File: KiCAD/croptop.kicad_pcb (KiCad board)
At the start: 4 copper layers, 152.4 x 53.3 mm, 286 parts, among them J1 PICKit Header, J2 USB_A, J3 5V USB, J4 4-1734839-0, J5 Terminal Block, J6 DNP, J7 DNP, SW1 BTNA, SW2 BTNA, SW3 BTNA, SW4 BTNA, U1 PIC32MX795F512L, U10 AD7799, U11 74HCT125D, U12 Si7006-A20, U13 UCAM-M8Q, U14 W25N01GV, U15 LIS3DH, U16 PUSBM5V5X4, U17 DT6250-06MR-13, U18 PUSBM5V5X4, U2 REG71055, U3 FAN5333BSX, U4 MIC23050, U5 TC1014, U6 FT812Q, U8 74HCT125D, U9 DRV8872, Y1 CXO, Y2 12MHz

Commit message: Dec 18th
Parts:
- removed C55: 100uF, Capacitor_SMD:CP_Elec_6.3x7.7
- removed C72: 0.1uF, Capacitor_SMD:C_0402_1005Metric
- removed R58, R59, R60, R61: 10k, Resistor_SMD:R_0402_1005Metric
- removed SW3, SW4: BTNA, Button_Switch_SMD:SW_SPST_PTS645
- removed TP93, TP94: TestPoint_Alt, TestPoint:TestPoint_Pad_D2.0mm
- D9: footprint Package_TO_SOT_SMD:TO-252-3_TabPin2 -> croptop:SizeOfThisLad
- moved R62 161.8 mm to (200.7, 84.5)
- moved R64 155.3 mm to (201.6, 66.5)
- moved R65 152.4 mm to (202.3, 69.0)
- moved R56 151.5 mm to (198.3, 84.0)
- moved R37 102.6 mm to (125.3, 122.0), turned to 270 degrees
- moved R67 94.2 mm to (200.5, 70.3)
- moved R66 88.8 mm to (199.3, 68.4)
- moved D9 86.3 mm to (117.1, 130.2), turned to 180 degrees
- moved R48 86.1 mm to (105.7, 125.5), turned to 180 degrees
- moved R63 85.3 mm to (200.7, 86.2)
- moved R36 83.9 mm to (125.3, 124.3), turned to 270 degrees
- moved R57 79.6 mm to (198.3, 86.4)
- moved U9 74.7 mm to (117.2, 123.1), turned to 180 degrees
- moved C42 74.5 mm to (206.7, 115.1)
- moved C47 73.7 mm to (122.9, 125.3), turned to 180 degrees
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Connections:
- U10 pad 5: Net-(C52-Pad1) -> Net-(C53-Pad1)
- U10 pad 6: Net-(C52-Pad2) -> Net-(C53-Pad2)
- U10 pad 7: Net-(C53-Pad1) -> Net-(C52-Pad1)
- U10 pad 8: Net-(C53-Pad2) -> Net-(C52-Pad2)
- U11 pad 2: Net-(R48-Pad1) -> ROT_A1
- U11 pad 3: ROT_A1 -> Net-(R48-Pad1)
- U11 pad 5: Net-(R49-Pad1) -> ROT_A2
- U11 pad 6: ROT_A2 -> Net-(R49-Pad1)
- U17 pad 3: Net-(J6-Pad4) -> ADC_A1-
- U17 pad 4: Net-(J6-Pad3) -> ADC_A1+
- U17 pad 5: ADC_A1- -> Net-(J6-Pad4)
- U17 pad 6: ADC_A1+ -> Net-(J6-Pad3)
- U5 pad 2: (no net) -> DRV_GND
- U6 pad 57: (no net) -> DRV_GND
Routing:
- net Net-(J7-Pad4): track 0.00 -> 25.4 mm, vias 0 -> 2
- net Net-(J7-Pad3): track 0.00 -> 24.4 mm, vias 0 -> 2
- net ROT_A2: track 0.00 -> 22.5 mm, vias 0 -> 6
- net ROT_VDD: track 0.00 -> 18.3 mm, vias 0 -> 2
- net ROT_A1: track 0.00 -> 16.9 mm, vias 0 -> 2
- net Net-(C54-Pad2): track 0.00 -> 15.8 mm, vias 0 -> 2
- net Net-(C54-Pad1): track 0.00 -> 15.6 mm, vias 0 -> 2
- net Net-(J6-Pad3): track 0.00 -> 11.7 mm, vias 0 -> 2
- net ADC_A1-: track 0.00 -> 11.3 mm, vias 0 -> 2
- net ADC_A1+: track 0.00 -> 10.2 mm, vias 0 -> 2
- net Net-(R39-Pad2): track 0.00 -> 10.1 mm, vias 0 -> 2
- net Net-(C52-Pad2): track 0.00 -> 9.97 mm, vias 0 -> 2
- net Net-(J4-Pad34): track 0.00 -> 9.70 mm
- net Net-(J4-Pad5): track 0.00 -> 9.65 mm
- net Net-(J4-Pad6): track 0.00 -> 9.36 mm
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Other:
- board size 152.4 x 53.3 mm -> 130.2 x 45.1 mm

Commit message: Dec 19th
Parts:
- moved C66 122.8 mm to (211.8, 118.1)
- moved C68 115.5 mm to (202.6, 127.0)
- moved U13 85.1 mm to (170.2, 103.5), turned to 180 degrees
- moved C42 77.5 mm to (135.0, 144.3)
- moved C41 77.5 mm to (132.2, 145.7)
- moved D22 73.7 mm to (146.6, 106.6)
- moved D24 73.7 mm to (142.2, 102.5)
- moved D25 73.7 mm to (142.5, 106.3)
- moved R64 73.7 mm to (138.1, 103.9)
- moved R65 73.7 mm to (138.8, 106.5)
- moved R66 73.7 mm to (135.8, 105.8)
- moved D23 73.7 mm to (146.0, 103.4)
- moved R67 73.7 mm to (137.0, 107.7)
- moved C3 61.9 mm to (108.1, 94.1)
- moved R27 61.9 mm to (115.1, 89.8)
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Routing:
- net LCD_G7: track 0.00 -> 30.3 mm, vias 0 -> 2
- net LCD_B6: track 0.00 -> 29.6 mm, vias 0 -> 2
- net LCD_DISP: track 0.00 -> 29.2 mm, vias 0 -> 2
- net LCD_DEN: track 0.00 -> 29.1 mm, vias 0 -> 2
- net LCD_SHIFT: track 0.00 -> 29.0 mm, vias 0 -> 2
- net LCD_B0: track 0.00 -> 29.0 mm, vias 0 -> 2
- net LCD_HSYNC: track 0.00 -> 29.0 mm, vias 0 -> 2
- net LCD_VSYNC: track 0.00 -> 28.8 mm, vias 0 -> 2
- net LCD_B7: track 0.00 -> 28.8 mm, vias 0 -> 2
- net LCD_B1: track 0.00 -> 28.8 mm, vias 0 -> 2
- net LCD_G6: track 0.00 -> 28.7 mm, vias 0 -> 2
- net LCD_B2: track 0.00 -> 28.5 mm, vias 0 -> 2
- net LCD_B3: track 0.00 -> 28.3 mm, vias 0 -> 2
- net LCD_B4: track 0.00 -> 28.1 mm, vias 0 -> 2
- net LCD_B5: track 0.00 -> 27.9 mm, vias 0 -> 2
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
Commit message: Before remove LCD resistors
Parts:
- moved R52 89.7 mm to (184.0, 94.7)
- moved R53 86.3 mm to (178.3, 91.6)
- moved C66 32.0 mm to (184.3, 101.9)
- moved C68 27.5 mm to (183.9, 106.8)
- moved C63 17.0 mm to (105.7, 124.0)
- moved C62 14.0 mm to (109.0, 123.7)
- moved C17 9.60 mm to (120.7, 85.9)
- moved C47 8.32 mm to (114.6, 125.2)
- moved U9 8.25 mm to (125.3, 121.7)
- moved R36 6.77 mm to (128.4, 118.3), turned to 180 degrees
- moved C42 6.51 mm to (131.6, 138.7), turned to 90 degrees
- moved R37 5.72 mm to (128.4, 117.2), turned to 180 degrees
- moved U6 4.42 mm to (141.9, 121.4)
- moved C33 4.32 mm to (151.2, 121.1)
- moved C34 4.32 mm to (150.1, 121.1)
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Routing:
- net Net-(C47-Pad1): track 0.00 -> 28.4 mm
- net DRV_GND: track 16.9 -> 42.4 mm
- net TCH_UP: track 10.4 -> 32.6 mm, vias 1 -> 2
- net VBUS: track 0.00 -> 21.9 mm, vias 0 -> 2
- net DRV_OUT1: track 0.00 -> 20.8 mm, vias 0 -> 2
- net TCH_LEFT: track 11.4 -> 31.8 mm, vias 1 -> 2
- net TCH_RIGHT: track 9.02 -> 29.4 mm, vias 1 -> 2
- net TCH_DOWN: track 12.5 -> 30.7 mm, vias 1 -> 2
- net SS2: track 16.3 -> 0.00 mm
- net LCD_R1: track 16.3 -> 0.00 mm, vias 2 -> 0
- net DRV_OUT2: track 0.00 -> 16.2 mm, vias 0 -> 2
- net SDO2: track 15.5 -> 0.00 mm
- net LCD_R0: track 15.4 -> 0.00 mm, vias 2 -> 0
- net SDIO2: track 14.7 -> 0.00 mm
- net SCLK2: track 13.9 -> 0.00 mm
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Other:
- net class Default: clearance 0.2 -> 0.127; trace_width 0.25 -> 0.127; via_dia 0.8 -> 0.508; via_drill 0.4 -> 0.254
- rule trace_clearance: 0.2 -> 0.127
- rule trace_min: 0.2 -> 0.127
- rule via_min_drill: 0.3 -> 0.254

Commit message: Before USB update
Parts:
- removed C41: 10uF, Capacitor_SMD:C_0805_2012Metric
- removed C42: 0.1uF, Capacitor_SMD:C_0402_1005Metric
- moved D2 71.7 mm to (158.5, 161.1), turned to 90 degrees
- moved R2 69.0 mm to (158.6, 154.0)
- moved R3 65.9 mm to (158.6, 152.7)
- moved D1 65.5 mm to (154.2, 151.4)
- moved C27 64.6 mm to (153.7, 154.6), turned to 270 degrees
- moved C28 63.5 mm to (158.5, 156.3)
- moved R28 63.2 mm to (158.5, 155.1)
- moved C31 62.8 mm to (158.5, 157.5)
- moved R4 62.1 mm to (158.6, 151.4)
- moved C16 59.8 mm to (157.8, 144.4)
- moved C21 57.1 mm to (155.0, 144.6)
- moved L2 53.6 mm to (153.3, 147.7), turned to 90 degrees
- moved U3 33.5 mm to (159.9, 120.5), turned to 90 degrees
- moved R62 21.7 mm to (179.3, 124.5)
- moved R63 21.7 mm to (179.8, 120.3)
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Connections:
- net BTN_C renamed Net-(U1-Pad22)
- net BTN_D renamed Net-(U1-Pad23)
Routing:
- net LCD_PD: track 0.00 -> 24.3 mm
- net LCD_INT: track 0.00 -> 23.3 mm
- net SS2: track 0.00 -> 20.3 mm
- net SDO2: track 0.00 -> 19.2 mm
- net SDIO2: track 0.00 -> 18.2 mm
- net SCLK2: track 0.00 -> 17.0 mm
- net LCD_R0: track 0.00 -> 7.75 mm, vias 0 -> 2
- net LCD_R1: track 0.00 -> 7.55 mm, vias 0 -> 2
- net DRV_GND: track 42.4 -> 38.1 mm, vias 1 -> 0
- net LCD_SHIFT: track 22.3 -> 24.8 mm
- net LCD_DISP: track 22.4 -> 24.9 mm
- net LCD_DEN: track 22.9 -> 24.9 mm
- net LCD_HSYNC: track 23.0 -> 24.9 mm
- net LCD_VSYNC: track 23.0 -> 24.8 mm
- net LCD_G7: track 19.5 -> 20.9 mm
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
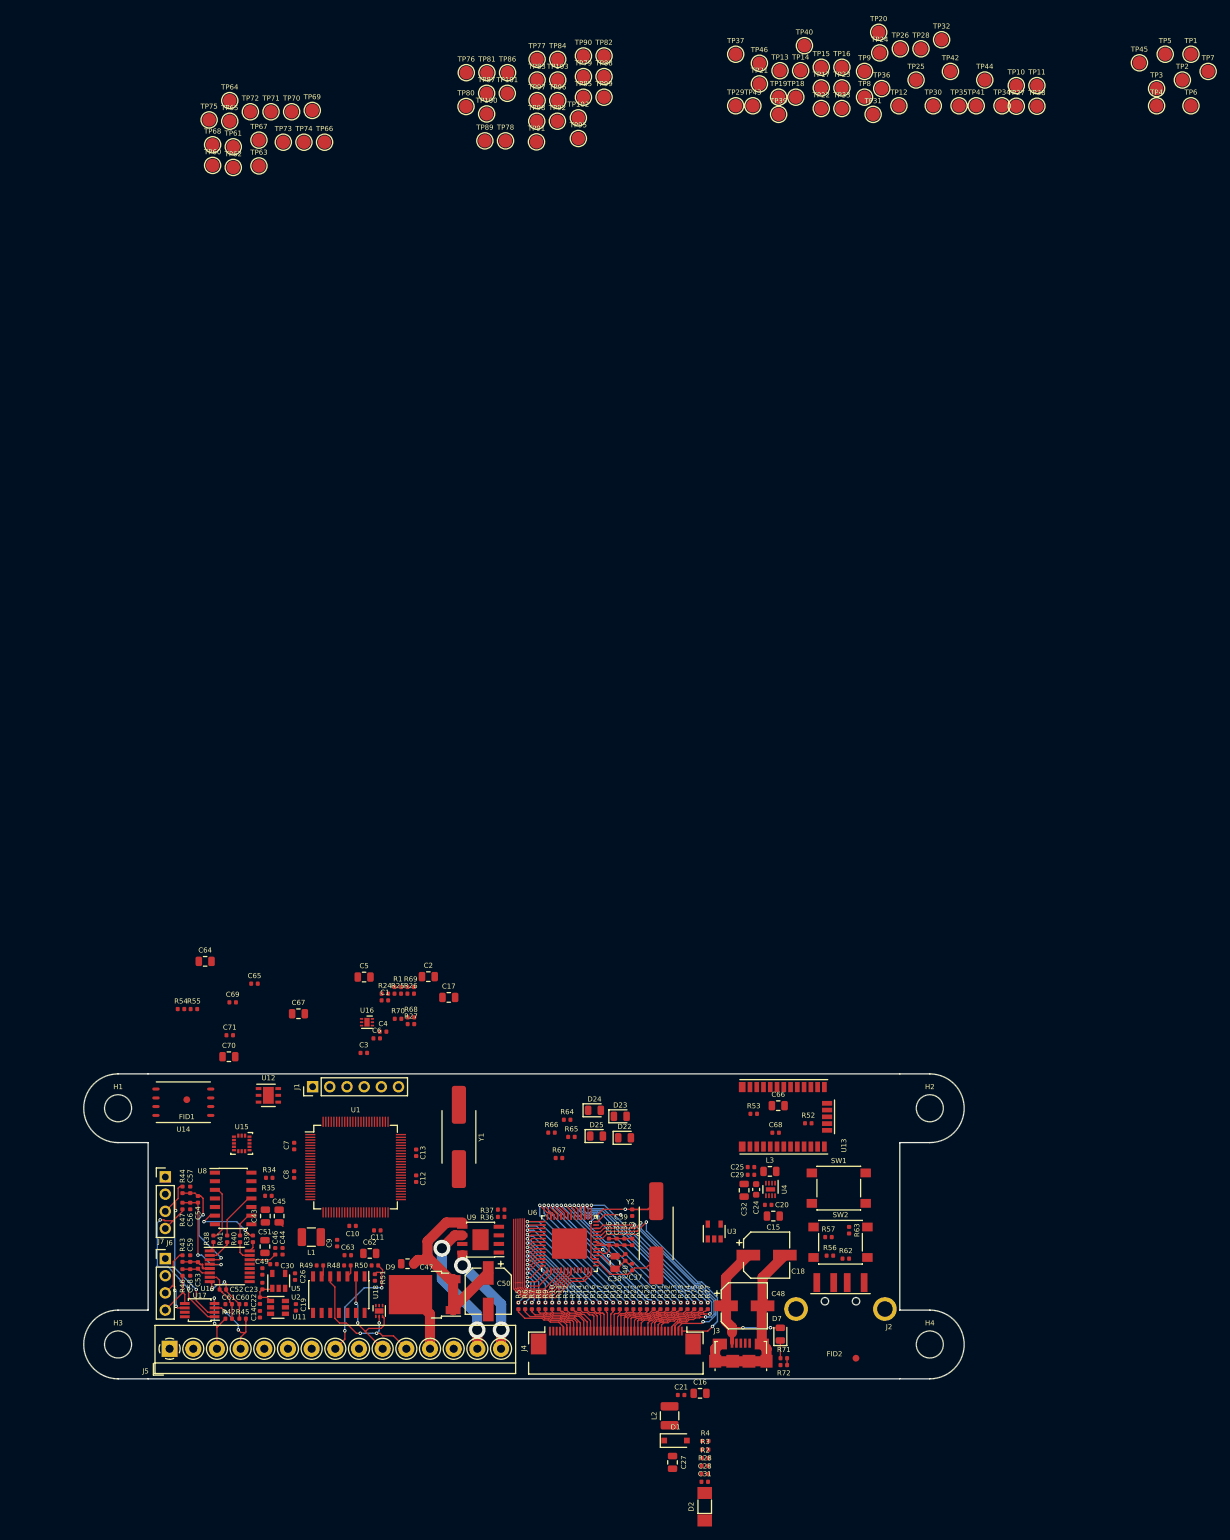
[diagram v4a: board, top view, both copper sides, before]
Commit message: Final board shape
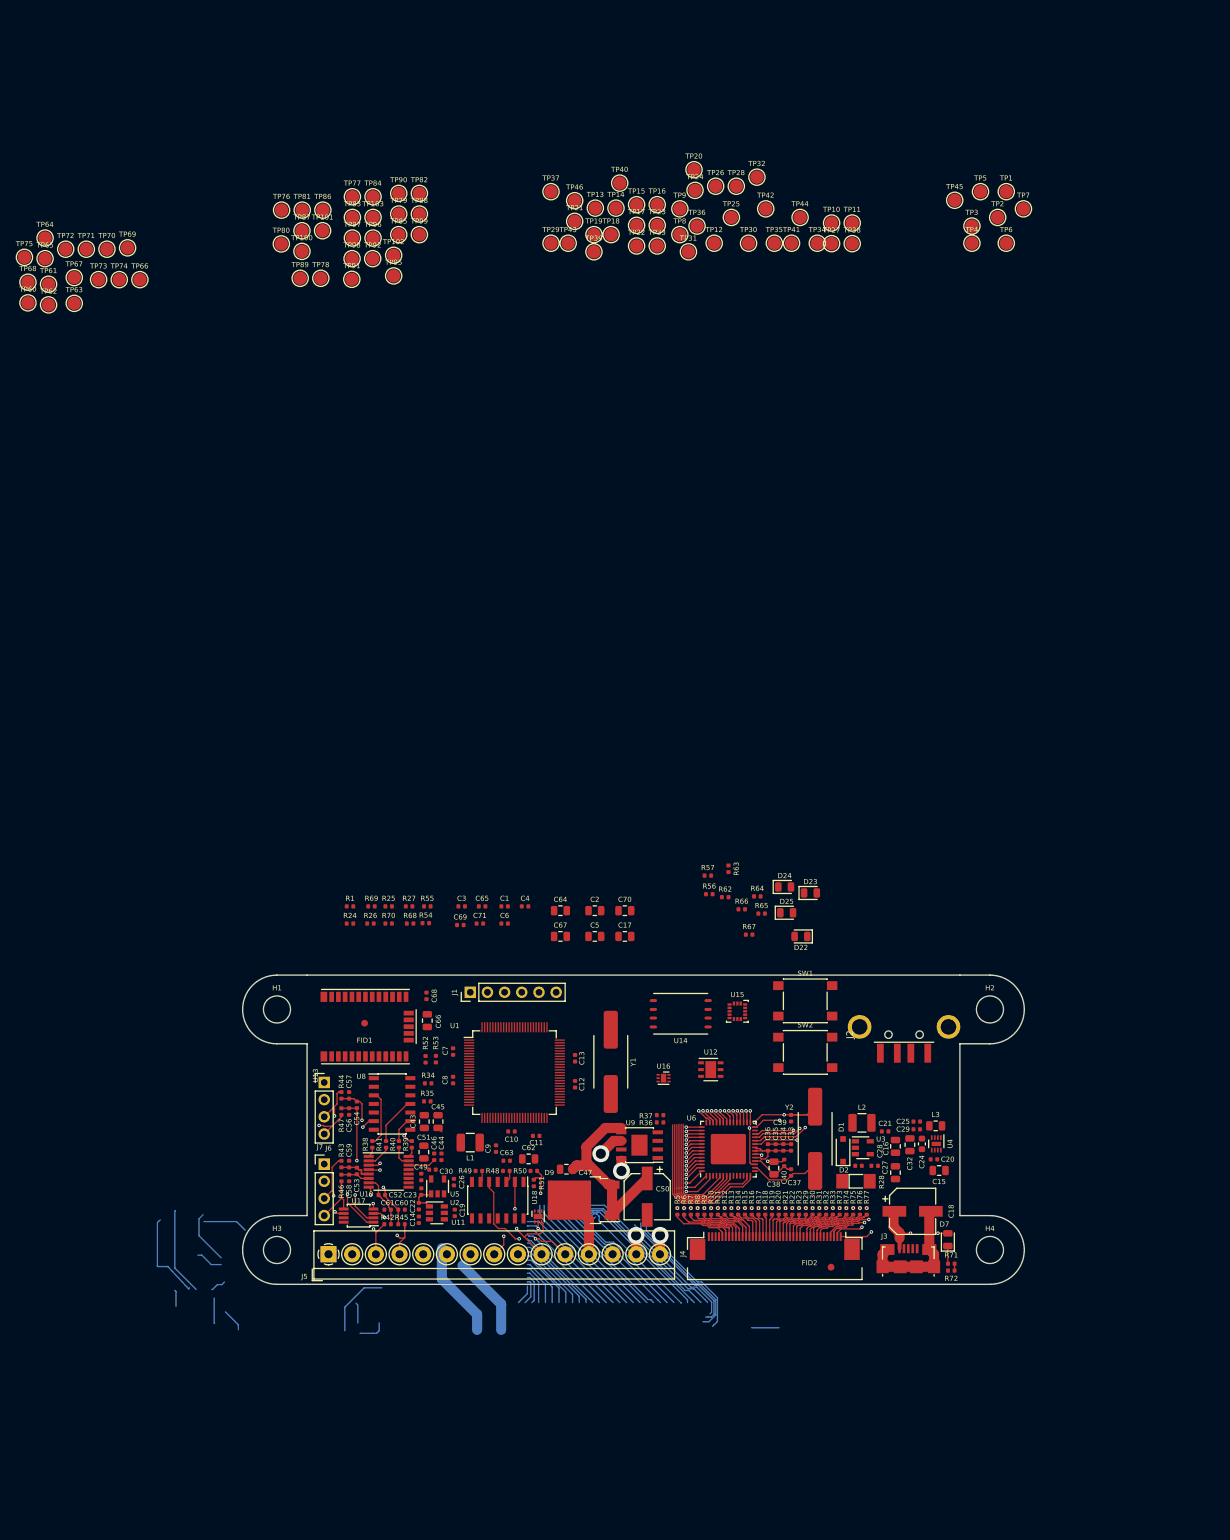
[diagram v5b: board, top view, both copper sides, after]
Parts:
- removed C31: 1uF, Capacitor_SMD:C_0402_1005Metric
- removed C48: 100uF, Capacitor_SMD:CP_Elec_6.3x7.7
- removed R2, R3, R4: 10, Resistor_SMD:R_0402_1005Metric
- R28: value 10 -> 2.2
- moved U15 75.8 mm to (163.3, 87.9)
- moved U14 74.7 mm to (154.9, 88.3)
- moved U12 65.5 mm to (159.4, 96.5)
- moved U13 63.3 mm to (108.3, 90.2)
- moved C70 62.4 mm to (146.7, 73.0)
- moved R52 57.4 mm to (117.2, 95.0), turned to 90 degrees
- moved R62 56.3 mm to (161.5, 71.0)
- moved R56 56.3 mm to (159.2, 70.6)
- moved R63 56.3 mm to (162.0, 66.8)
- moved R57 56.3 mm to (159.0, 67.8)
- moved C68 55.4 mm to (117.3, 85.6), turned to 270 degrees
- moved C27 54.0 mm to (186.7, 111.8)
- moved J2 54.0 mm to (188.0, 84.5), turned to 90 degrees
- moved C66 53.4 mm to (117.5, 89.3), turned to 90 degrees
- moved C64 53.1 mm to (137.2, 73.0)
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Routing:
- net ROT_A2: track 21.6 -> 53.8 mm
- net DRV_GND: track 38.1 -> 65.4 mm
- net DRV_OUT1: track 20.8 -> 44.3 mm
- net TCH_LEFT: track 32.5 -> 11.7 mm
- net LCD_B5: track 22.7 -> 2.12 mm
- net TCH_DOWN: track 31.5 -> 11.7 mm
- net DRV_OUT2: track 16.2 -> 36.0 mm
- net LCD_G6: track 19.7 -> 2.34 mm
- net TCH_RIGHT: track 30.4 -> 13.6 mm
- net LCD_G4: track 17.3 -> 2.45 mm
- net ROT_A1: track 16.9 -> 29.5 mm
- net LCD_G2: track 15.2 -> 2.56 mm
- net VBUS: track 21.9 -> 13.1 mm
- net Net-(C38-Pad1): track 5.35 -> 4.08 mm
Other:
- board size 130.2 x 45.1 mm -> 115.6 x 45.7 mm

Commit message: Finished working board
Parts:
- removed C29: 1uF, Capacitor_SMD:C_0402_1005Metric
- removed C62, C64, C66, C67, C70: 10uF, Capacitor_SMD:C_0805_2012Metric
- removed D22: LED4, LED_SMD:LED_0805_2012Metric
- removed D23: LED3, LED_SMD:LED_0805_2012Metric
- removed R48, R49, R68, R69: 10, Resistor_SMD:R_0402_1005Metric
- removed R64, R65: 60, Resistor_SMD:R_0402_1005Metric
- removed TP101, TP102, TP103, TP4, TP63, TP67, TP69, TP75, TP81, TP84, TP87, TP95, TP98: TestPoint_Alt, TestPoint:TestPoint_Pad_D2.0mm
- H1, H2, H3, H4: footprint MountingHole:MountingHole_4mm -> MountingHole:MountingHole_4mm_Pad
- moved TP1 130.7 mm to (135.8, 78.8)
- moved TP5 127.7 mm to (132.8, 75.8)
- moved TP2 127.5 mm to (129.7, 75.8)
- moved TP7 127.3 mm to (135.8, 75.8)
- moved TP3 126.9 mm to (129.7, 78.8)
- moved TP6 125.9 mm to (132.8, 78.8)
- moved TP45 125.3 mm to (120.2, 68.2)
- moved TP32 124.2 mm to (108.0, 74.3)
- moved TP10 120.3 mm to (101.9, 65.2)
- moved TP28 120.3 mm to (111.0, 74.3)
- moved TP27 119.9 mm to (98.8, 65.2)
- moved TP64 118.7 mm to (104.9, 83.9)
- moved TP11 118.0 mm to (104.9, 62.1)
- moved TP65 117.6 mm to (101.9, 86.9)
- moved TP38 117.3 mm to (114.1, 71.3)
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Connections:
- C10 pad 1: LIN_VDD -> DVDD
- C11 pad 1: LIN_VDD -> DVDD
- C12 pad 1: LIN_VDD -> DVDD
- C13 pad 1: LIN_VDD -> DVDD
- C14 pad 1: VBUS -> DVDD_UNREG
- C15 pad 1: VBUS -> DVDD_UNREG
- C16 pad 1: VBUS -> DVDD_UNREG
- C17 pad 1: VBUS -> DVDD_UNREG
- C18 pad 1: VBUS -> DVDD_UNREG
- C20 pad 1: VBUS -> DVDD_UNREG
- C21 pad 1: VBUS -> DVDD_UNREG
- C24 pad 2: LIN_VDD -> DVDD
- C25 pad 1: LIN_VDD -> DVDD
- C3 pad 1: LIN_VDD -> DVDD
- C32 pad 1: LIN_VDD -> DVDD
- C33 pad 1: LIN_VDD -> DVDD
- C34 pad 1: LIN_VDD -> DVDD
- C35 pad 1: LIN_VDD -> DVDD
- C36 pad 1: LIN_VDD -> DVDD
- C43 pad 1: LIN_VDD -> DVDD
- C44 pad 1: LIN_VDD -> DVDD
- C45 pad 1: LIN_VDD -> DVDD
- C46 pad 1: LIN_VDD -> DVDD
- C5 pad 1: LIN_VDD -> DVDD
- C63 pad 1: LIN_VDD -> DVDD
- C65 pad 1: LIN_VDD -> DVDD
- C68 pad 1: LIN_VDD -> DVDD
- C69 pad 1: LIN_VDD -> DVDD
- C7 pad 1: LIN_VDD -> DVDD
- C71 pad 1: LIN_VDD -> DVDD
- C8 pad 1: LIN_VDD -> DVDD
- C9 pad 1: LIN_VDD -> DVDD
- D7 pad 2: VBUS -> DVDD_UNREG
- J1 pad 2: LIN_VDD -> DVDD
- J1 pad 4: Net-(J1-Pad4) -> PKT_PGED
- J1 pad 5: Net-(J1-Pad5) -> PKT_PGEC
- J2 pad 1: VBUS -> DVDD_UNREG
- J3 pad 1: VBUS -> DVDD_UNREG
- J4 pad 4: LIN_VDD -> DVDD
- J5 pad 5: LIN_VDD -> DVDD
- L1 pad 1: LIN_VDD -> DVDD
- L2 pad 2: VBUS -> DVDD_UNREG
- L3 pad 1: LIN_VDD -> DVDD
- R1 pad 1: LIN_VDD -> DVDD
- R24 pad 1: LIN_VDD -> DVDD
- R25 pad 1: LIN_VDD -> DVDD
- R50 pad 1: LIN_VDD -> DVDD
- R51 pad 2: VBUS -> DVDD_UNREG
- SW1 pad 2: Net-(R56-Pad2) -> DVDD
- SW2 pad 2: Net-(R57-Pad2) -> DVDD
- TP1 pad 1: LIN_VDD -> DVDD
- TP5 pad 1: VBUS -> DVDD_UNREG
- U1 pad 16: LIN_VDD -> DVDD
- U1 pad 19: LCD_INT -> GPS_INT
- U1 pad 2: LIN_VDD -> DVDD
- U1 pad 20: BTN_A -> Net-(U1-Pad20)
- U1 pad 21: BTN_B -> Net-(U1-Pad21)
- U1 pad 32: GPS_INT -> Net-(U1-Pad32)
- U1 pad 37: LIN_VDD -> DVDD
- U1 pad 46: LIN_VDD -> DVDD
- U1 pad 54: VBUS -> DVDD_UNREG
- U1 pad 55: LIN_VDD -> DVDD
- U1 pad 62: LIN_VDD -> DVDD
- U1 pad 73: Net-(U1-Pad73) -> BTN_B
- U1 pad 74: Net-(U1-Pad74) -> BTN_A
- U1 pad 8: LED_C -> Net-(U1-Pad8)
- U1 pad 86: LIN_VDD -> DVDD
- U1 pad 9: LED_D -> Net-(U1-Pad9)
- U10 pad 14: LIN_VDD -> DVDD
- U11 pad 14: LIN_VDD -> DVDD
- U11 pad 3: Net-(R48-Pad1) -> ROT_Y1
- U11 pad 6: Net-(R49-Pad1) -> ROT_Y2
- U12 pad 5: LIN_VDD -> DVDD
- U13 pad 1: LIN_VDD -> DVDD
- U13 pad 8: LIN_VDD -> DVDD
- U13 pad 9: LIN_VDD -> DVDD
- U14 pad 8: LIN_VDD -> DVDD
- U15 pad 1: LIN_VDD -> DVDD
- U15 pad 14: LIN_VDD -> DVDD
- U15 pad 7: LIN_VDD -> DVDD
- U15 pad 8: LIN_VDD -> DVDD
- U16 pad 6: VBUS -> DVDD_UNREG
- U18 pad 6: LIN_VDD -> DVDD_UNREG
- U2 pad 3: VBUS -> DVDD_UNREG
- U2 pad 5: VBUS -> DVDD_UNREG
- U3 pad 5: VBUS -> DVDD_UNREG
- U4 pad 2: VBUS -> DVDD_UNREG
- U4 pad 4: LIN_VDD -> DVDD
- U4 pad 7: VBUS -> DVDD_UNREG
- U6 pad 11: LIN_VDD -> DVDD
- U6 pad 19: LIN_VDD -> DVDD
- U6 pad 21: LIN_VDD -> DVDD
- U6 pad 22: LIN_VDD -> DVDD
- U8 pad 14: LIN_VDD -> DVDD
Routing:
- net DRV_GND: track 65.4 -> 260.9 mm, vias 0 -> 91
- net DVDD: track 0.00 -> 148.8 mm, vias 0 -> 38
- net DVDD_UNREG: track 0.00 -> 116.2 mm, vias 0 -> 9
- net USB_D+: track 0.00 -> 92.2 mm, vias 0 -> 2
- net USB_D-: track 0.00 -> 92.1 mm, vias 0 -> 2
- net LED_B: track 0.00 -> 71.0 mm, vias 0 -> 8
- net LED_A: track 0.00 -> 66.7 mm, vias 0 -> 8
- net SCL: track 0.00 -> 64.4 mm, vias 0 -> 6
- net SDA: track 0.00 -> 61.4 mm
- net BTN_A: track 0.00 -> 57.6 mm, vias 0 -> 2
- net LCD_CATHODE: track 0.00 -> 54.5 mm, vias 0 -> 2
- net LCD_ANODE: track 0.00 -> 53.9 mm, vias 0 -> 4
- net SCLK: track 0.00 -> 52.9 mm, vias 0 -> 10
- net ADC_GND: track 0.00 -> 51.7 mm, vias 0 -> 2
- net BTN_B: track 0.00 -> 48.6 mm, vias 0 -> 2
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- added copper zone on Vdd.Cu, net ADC_VDD
- added copper zone on Gnd.Cu, net DRV_GND
- added copper zone on Vdd.Cu, net DVDD
- added copper zone on Vdd.Cu, net DVDD_UNREG
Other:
- outline, holes or cut-outs redrawn
- board text added: "1Gb NAND FLASH"
- board text added: "BOARD MODEL:"
- board text added: "BTN A"
- board text added: "BTN B"
- board text added: "BY KENNEDY CAISLEY & RYAN DONAHUE"
- board text added: "CROPTOP v1.0"
- board text added: "DATA ACQUISITION PLATFORM"
- board text added: "DESIGNED AT THE UNIVERSITY OF IDAHO"
- board text added: "FOR AGRICULTURE RESEARCH"
- board text added: "GNSS Reciever"
- board text added: "IO Terminal Block"
- board text added: "PIC32MX"
- board text added: "PICKit3"
- board text added: "TFT LCD"
- board text added: "USB 2.0"
- board text added: "USB 5V"
- board text added: "ΔΣ ADC"
